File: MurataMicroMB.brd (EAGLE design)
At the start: 90 x 63 mm, 63 parts, among them CON1 C-2395, CON2 WM17143CT-ND, CON3 CON_MIL_10_ARM, CON4 C-2395, IC1 NC7SZ00M5XCT-ND, IC2 296-35164-1-ND, IC3 IC_LPC11U3XQFN33, IC4 AZ1117EH-3.3TRG1DICT-ND, Q1 1253-1168-1-ND, SW1 P-8073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

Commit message: update eagle version = 7.5.0; library update
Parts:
- CON1, CON4: value C-2395 -> CON_MICROSD_C2395
- IC4: value AZ1117EH-3.3TRG1DICT-ND -> LDO4_3.3_SOT223
- L1: value 445-7844-1-ND -> INDUCTOR_4.7U_2016
- moved D1 7.96 mm to (51.5, 17.9), turned to 180 degrees
- moved L1 6.41 mm to (48.1, 21.4), turned to 270 degrees
- moved C6 4.68 mm to (56.8, 19.0), turned to 90 degrees
- moved C4 4.50 mm to (44.8, 21.7)
- moved X1 4.50 mm to (41.1, 21.9)
- moved C7 4.50 mm to (46.4, 21.6)
- moved R2 4.26 mm to (51.0, 24.4), turned to 180 degrees
- moved TP8 3.20 mm to (61.0, 15.5)
- moved TP9 3.20 mm to (65.0, 15.5)
- moved IC2 3.04 mm to (51.0, 21.5), turned to 0 degrees
- moved R3 2.78 mm to (55.5, 19.0), turned to 270 degrees
- moved R4 2.33 mm to (54.3, 20.8), turned to 270 degrees
- moved C5 1.55 mm to (58.3, 19.1), turned to 90 degrees
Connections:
- net N$7: now also IC2.1; no longer IC2.5
- net VIN: now also IC2.5; no longer IC2.1
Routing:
- net N$8: track 12.3 -> 1.44 mm, vias 2 -> 0
- net GND: track 20.4 -> 11.8 mm, vias 21 -> 19
- net VBUS: track 47.2 -> 42.8 mm
- net VPP: track 21.7 -> 23.2 mm
- net N$7: track 5.20 -> 4.14 mm
- net N$10: track 5.55 -> 4.85 mm

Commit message: library update
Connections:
- net !CS!: no longer R5.2
- net SCK: now also R5.2
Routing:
- net SCK: track 23.1 -> 33.0 mm, vias 0 -> 2
- net !CS!: track 16.4 -> 11.6 mm
- net MOSI: track 16.0 -> 17.7 mm
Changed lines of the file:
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@@
 <contactref element="CON1" pad="CLK"/>
 <wire x1="43.25" y1="27.55" x2="43.6" y2="27.2" width="0.25" layer="1"/>
-<wire x1="43.6" y1="27.2" x2="59.7" y2="27.2" width="0.25" layer="1"/>
+<wire x1="43.6" y1="27.2" x2="57.3" y2="27.2" width="0.25" layer="1"/>
+<wire x1="57.3" y1="27.2" x2="59.7" y2="27.2" width="0.25" layer="1"/>
 <wire x1="59.7" y1="27.2" x2="62.8" y2="30.3" width="0.25" layer="1"/>
 <wire x1="63.6" y1="30.3" x2="62.8" y2="30.3" width="0.25" layer="1"/>
 <contactref element="IC3" pad="23"/>
 <wire x1="43.25" y1="27.55" x2="43.25" y2="28.85" width="0.25" layer="1"/>
+<contactref element="R5" pad="2"/>
+<wire x1="54" y1="33.6" x2="56.9" y2="33.6" width="0.25" layer="1"/>
+<wire x1="56.9" y1="33.6" x2="57.3" y2="33.2" width="0.25" layer="1"/>
+<via x="57.3" y="33.2" extent="1-16" drill="0.3"/>
+<wire x1="57.3" y1="33.2" x2="57.3" y2="27.5" width="0.25" layer="16"/>
+<via x="57.3" y="27.2" extent="1-16" drill="0.3"/>
+<wire x1="57.3" y1="27.5" x2="57.3" y2="27.2" width="0.25" layer="16"/>
+<wire x1="57.2" y1="27.4" x2="57.3" y2="27.5" width="0.25" layer="16"/>
+<wire x1="57.3" y1="27.5" x2="57.4" y2="27.4" width="0.25" layer="16"/>
+<wire x1="57.4" y1="27.4" x2="57.4" y2="27.3" width="0.25" layer="16"/>
+<wire x1="57.2" y1="27.4" x2="57.2" y2="27.3" width="0.25" layer="16"/>
 </signal>
 <signal name="MISO">
@@
 <wire x1="63.6" y1="28.1" x2="61.4" y2="28.1" width="0.25" layer="1"/>
 <wire x1="61.4" y1="28.1" x2="60" y2="26.7" width="0.25" layer="1"/>
-<wire x1="60" y1="26.7" x2="43.4" y2="26.7" width="0.25" layer="1"/>
-<wire x1="43.4" y1="26.7" x2="42.75" y2="27.35" width="0.25" layer="1"/>
+<wire x1="60" y1="26.7" x2="57.7" y2="26.7" width="0.25" layer="1"/>
+<wire x1="57.7" y1="26.7" x2="57.5" y2="26.5" width="0.25" layer="1"/>
+<wire x1="57.5" y1="26.5" x2="43.6" y2="26.5" width="0.25" layer="1"/>
+<wire x1="43.6" y1="26.5" x2="42.75" y2="27.35" width="0.25" layer="1"/>
 <contactref element="IC3" pad="22"/>
 <wire x1="42.75" y1="27.35" x2="42.75" y2="28.85" width="0.25" layer="1"/>
@@
 <wire x1="63.6" y1="32.5" x2="63.2" y2="32.5" width="0.25" layer="1"/>
 <wire x1="63.2" y1="32.5" x2="63.1" y2="32.4" width="0.25" layer="1"/>
-<wire x1="63.1" y1="32.4" x2="58.4" y2="32.4" width="0.25" layer="1"/>
-<wire x1="58.4" y1="32.4" x2="58.1" y2="32.4" width="0.25" layer="1"/>
-<wire x1="54" y1="32.4" x2="56.4" y2="32.4" width="0.25" layer="1"/>
-<via x="56.4" y="32.4" extent="1-16" drill="0.3"/>
-<wire x1="56.4" y1="32.4" x2="58.1" y2="32.4" width="0.25" layer="16"/>
-<via x="58.1" y="32.4" extent="1-16" drill="0.3"/>
-<wire x1="58.1" y1="31.1" x2="58.1" y2="32.1" width="0.25" layer="1"/>
-<wire x1="58.1" y1="32.1" x2="58.1" y2="32.4" width="0.25" layer="1"/>
-<wire x1="58.4" y1="32.4" x2="58.1" y2="32.1" width="0.25" layer="1"/>
+<wire x1="63.1" y1="32.4" x2="60.1" y2="32.4" width="0.25" layer="1"/>
+<wire x1="60.1" y1="32.4" x2="59.8" y2="32.4" width="0.25" layer="1"/>
+<wire x1="54" y1="32.4" x2="58.6" y2="32.4" width="0.25" layer="1"/>
+<via x="58.6" y="32.4" extent="1-16" drill="0.3"/>
+<wire x1="58.6" y1="32.4" x2="59.8" y2="32.4" width="0.25" layer="16"/>
+<via x="59.8" y="32.4" extent="1-16" drill="0.3"/>
+<wire x1="59.8" y1="31.1" x2="59.8" y2="32.1" width="0.25" layer="1"/>
+<wire x1="59.8" y1="32.1" x2="59.8" y2="32.4" width="0.25" layer="1"/>
+<wire x1="60.1" y1="32.4" x2="59.8" y2="32.1" width="0.25" layer="1"/>
 <contactref element="R16" pad="2"/>
-<wire x1="54" y1="29.9" x2="56.9" y2="29.9" width="0.25" layer="1"/>
-<wire x1="56.9" y1="29.9" x2="58.1" y2="31.1" width="0.25" layer="1"/>
+<wire x1="54" y1="29.9" x2="58.6" y2="29.9" width="0.25" layer="1"/>
+<wire x1="58.6" y1="29.9" x2="59.8" y2="31.1" width="0.25" layer="1"/>
 </signal>
 <signal name="!CS!">
 <contactref element="CON1" pad="DAT3/CD"/>
-<contactref element="R5" pad="2"/>
-<wire x1="63.6" y1="33.6" x2="57.6" y2="33.6" width="0.25" layer="1"/>
-<wire x1="57.6" y1="33.6" x2="57.3" y2="33.6" width="0.25" layer="1"/>
-<wire x1="57.3" y1="33.6" x2="57" y2="33.6" width="0.25" layer="1"/>
-<wire x1="57" y1="33.6" x2="54" y2="33.6" width="0.25" layer="1"/>
-<wire x1="57.3" y1="31.6" x2="57.3" y2="33.3" width="0.25" layer="1"/>
-<wire x1="57.3" y1="33.3" x2="57.3" y2="33.6" width="0.25" layer="1"/>
-<wire x1="57" y1="33.6" x2="57.1" y2="33.5" width="0.25" layer="1"/>
-<wire x1="57.1" y1="33.5" x2="57.3" y2="33.3" width="0.25" layer="1"/>
-<wire x1="57.3" y1="33.3" x2="57.5" y2="33.5" width="0.25" layer="1"/>
-<wire x1="57.5" y1="33.5" x2="57.6" y2="33.6" width="0.25" layer="1"/>
-<wire x1="57.1" y1="33.5" x2="57.5" y2="33.5" width="0.25" layer="1"/>
+<wire x1="63.6" y1="33.6" x2="59.5" y2="33.6" width="0.25" layer="1"/>
+<wire x1="59.2" y1="31.6" x2="59.2" y2="33.3" width="0.25" layer="1"/>
+<wire x1="59.2" y1="33.3" x2="59.5" y2="33.6" width="0.25" layer="1"/>
 <contactref element="R15" pad="2"/>
-<wire x1="54" y1="31.1" x2="56.8" y2="31.1" width="0.25" layer="1"/>
-<wire x1="56.8" y1="31.1" x2="57.3" y2="31.6" width="0.25" layer="1"/>
+<wire x1="54" y1="31.1" x2="58.7" y2="31.1" width="0.25" layer="1"/>
+<wire x1="58.7" y1="31.1" x2="59.2" y2="31.6" width="0.25" layer="1"/>
 </signal>
 <signal name="VPP">

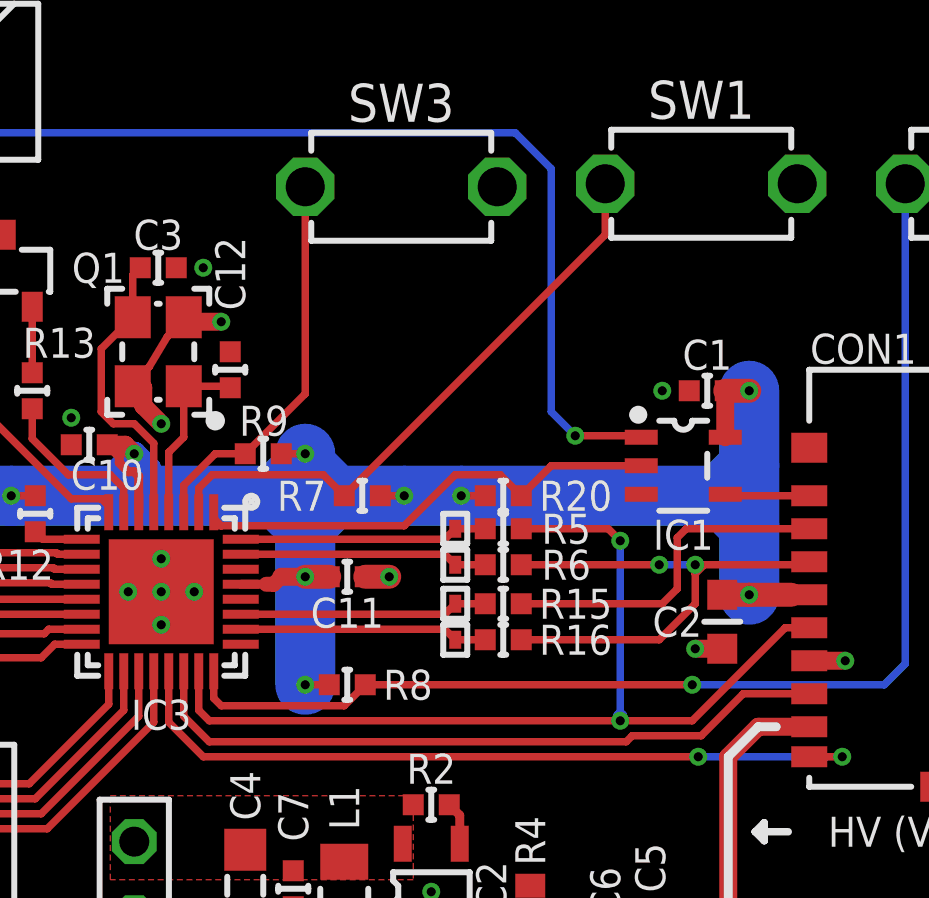
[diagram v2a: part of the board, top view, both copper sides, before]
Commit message: [ MB ] TP1,2,6,7 changed to use test pin; related Rs movee
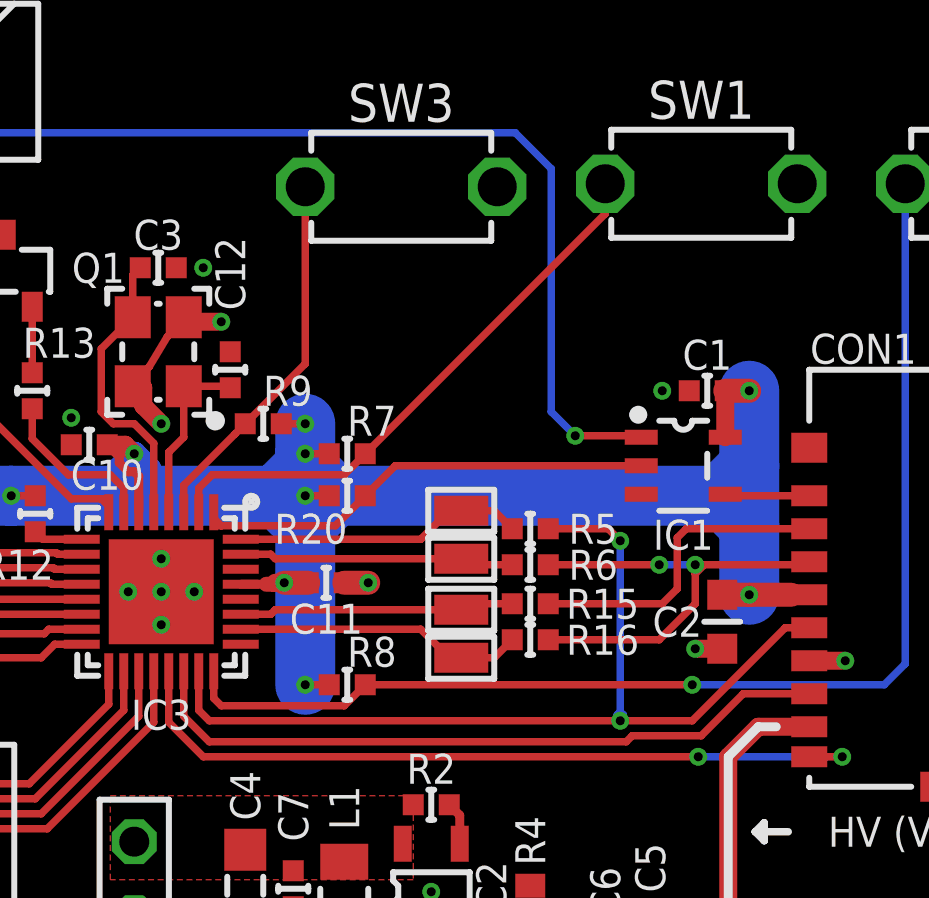
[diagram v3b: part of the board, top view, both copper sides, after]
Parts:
- TP1, TP2, TP6, TP7: value TESTPAD -> TESTPAD_1608; device mylib:TP06RECT -> mylib:TP_1608
- moved R20 5.20 mm to (48.2, 34.7)
- moved R7 1.49 mm to (48.2, 36.1), turned to 0 degrees
- moved R9 1.00 mm to (45.4, 37.1)
- moved R15 0.90 mm to (54.3, 31.1)
- moved R16 0.90 mm to (54.3, 29.9)
- moved R5 0.90 mm to (54.3, 33.6)
- moved R6 0.90 mm to (54.3, 32.4)
- moved C11 0.73 mm to (47.5, 31.8)
- moved TP7 0.63 mm to (52.0, 34.2)
- moved TP1 0.63 mm to (52.0, 29.3)
- moved TP2 0.28 mm to (52.0, 30.9)
- moved TP6 0.28 mm to (52.0, 32.6)
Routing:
- net MOSI: track 17.7 -> 15.9 mm
- net N$9: track 8.29 -> 9.69 mm
- net N$17: track 8.29 -> 9.69 mm
- net !RESET!: track 20.1 -> 19.1 mm
- net 3.3V: track 120.1 -> 121.0 mm
- net N$6: track 8.29 -> 9.19 mm
- net N$18: track 8.29 -> 9.19 mm
- net !CS!: track 11.6 -> 10.7 mm
- net SCK: track 33.0 -> 32.1 mm
- net ISP: track 13.1 -> 12.5 mm
- net TGT_RST: track 16.2 -> 15.6 mm
